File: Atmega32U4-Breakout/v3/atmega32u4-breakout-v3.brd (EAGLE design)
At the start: 39.1 x 21.3 mm, 57 parts, among them IC1 REG1117, U1 ATMEGA32U4

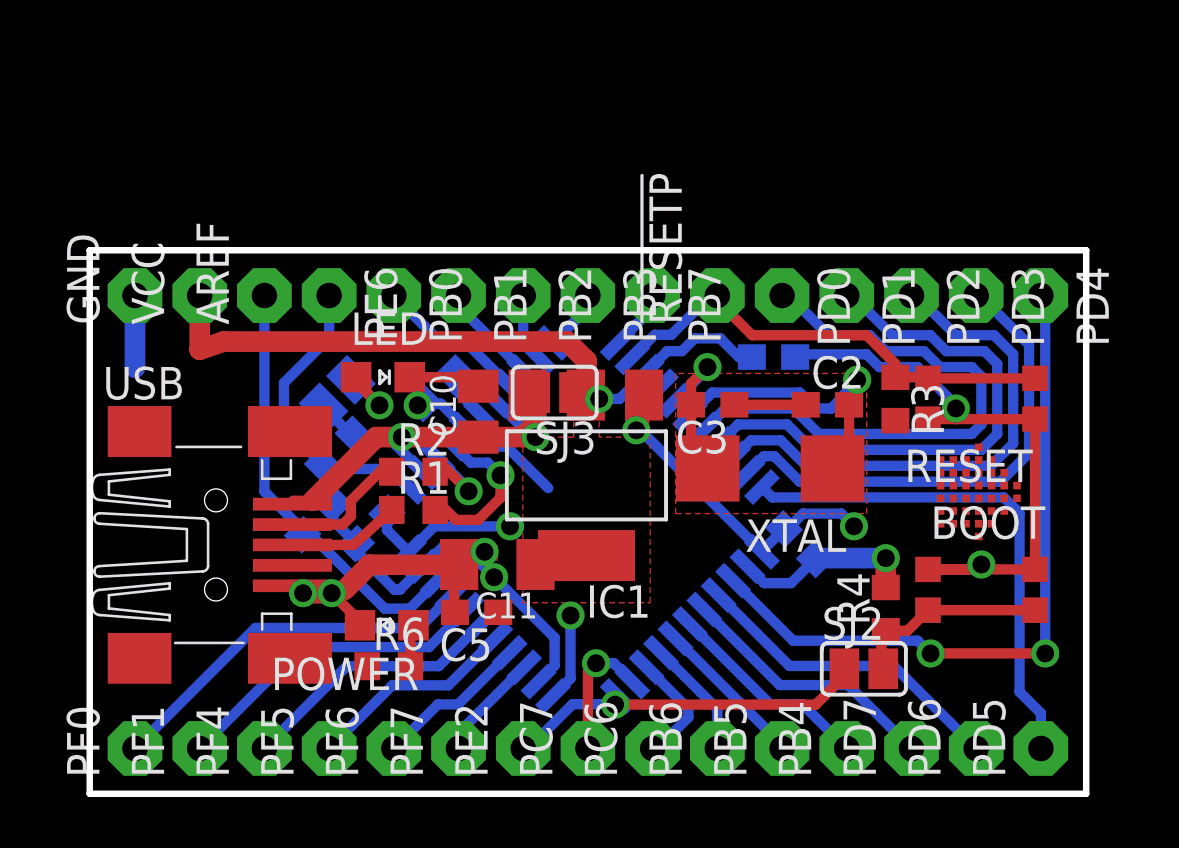
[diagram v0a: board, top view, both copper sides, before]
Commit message: Change button model, make vias smaller, adapt to multi-circuit-boards design rules, lots of small routing changes
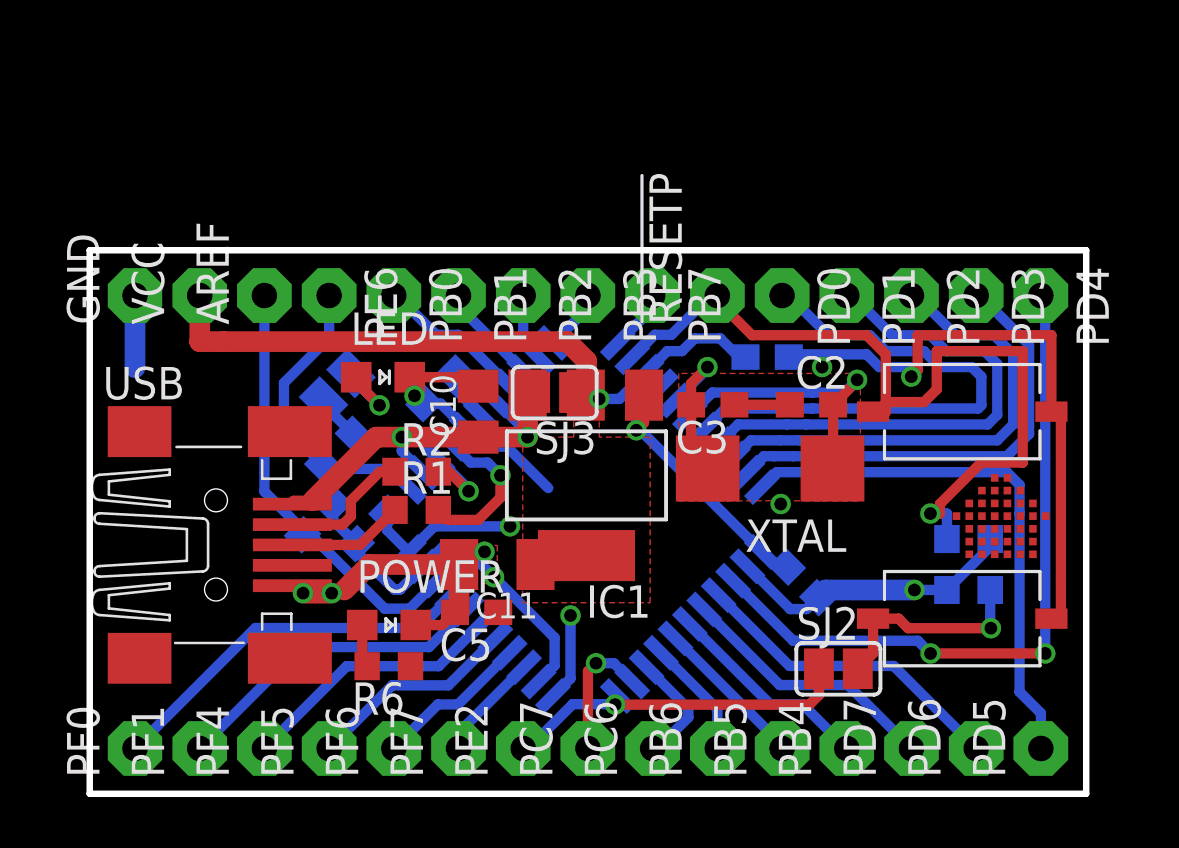
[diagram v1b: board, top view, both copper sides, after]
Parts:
- removed BOOT, RESET: SMDSWITCHKMR2NG, jocki:KMR2NG
- added BOOT1, RESET1: SMDSWITCHEDRAGON1, jocki:EDRAGON1
- moved R3 6.21 mm to (34.5, 10.0), flipped to the bottom, turned to 180 degrees
- moved R4 3.34 mm to (34.5, 8.00), flipped to the bottom, turned to 0 degrees
- moved C8 1.51 mm to (28.0, 8.30)
- moved SJ2 1.00 mm to (29.4, 4.91)
- moved C2 0.62 mm to (28.3, 15.3)
- moved C6 0.25 mm to (26.6, 17.1)
- moved SJ1 0.25 mm to (9.72, 16.0)
- moved R1 0.12 mm to (12.8, 11.1)
- moved R2 0.12 mm to (12.8, 12.6)
- moved POWER 0.09 mm to (11.8, 6.62), turned to 270 degrees
- turned R6 to 180 degrees
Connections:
- net !RESET: now also RESET1.P$2; no longer RESET.B1, RESET.B2
- net GND: now also BOOT1.P$1, RESET1.P$1; no longer BOOT.A1, BOOT.A2, RESET.A1, RESET.A2
- net N$21: now also BOOT1.P$2; no longer BOOT.B1, BOOT.B2
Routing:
- net !RESET: track 18.6 -> 32.9 mm, vias 0 -> 1
- net GND: track 81.2 -> 74.6 mm
- net VCC: track 43.9 -> 47.5 mm
- net VUSB: track 17.6 -> 16.1 mm
- net N$30: track 19.3 -> 18.1 mm
- net N$29: track 20.5 -> 19.2 mm
- net N$27: track 22.8 -> 21.5 mm
- net N$28: track 21.7 -> 20.4 mm
- net N$5: track 12.3 -> 11.0 mm
- net N$12: track 20.1 -> 21.3 mm
- net !HWB: track 14.5 -> 14.0 mm
- net N$21: track 8.29 -> 8.51 mm, vias 0 -> 1
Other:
- board text removed: "BOOT_EN"

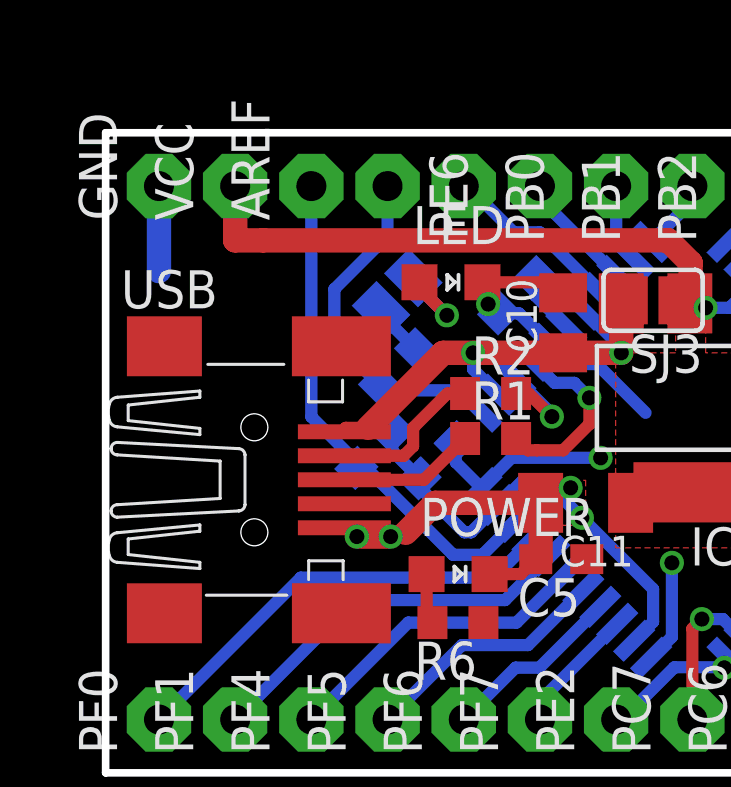
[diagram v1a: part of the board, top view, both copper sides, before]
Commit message: change USB plug package, rearrange bottom solder jumper
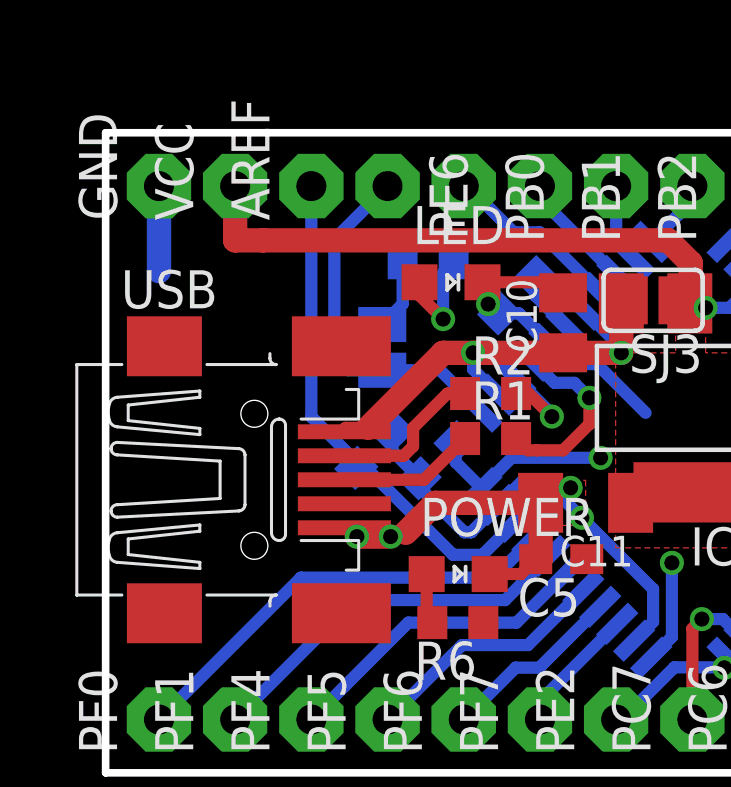
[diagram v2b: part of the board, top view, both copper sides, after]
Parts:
- USB: value MINI-USB-HIROSE-NOVIA -> MINI-USB-32005-201; device jocki:SMD-HIROSE-NOVIA -> jocki:32005-201
- moved R5 3.63 mm to (10.8, 17.0), turned to 180 degrees
- moved SJ1 1.84 mm to (9.22, 14.2), turned to 90 degrees
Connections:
- removed net N$4: R5.2, SJ1.1
- new net N$22: LED.A, R5.2
- net LED: now also SJ1.1; no longer R5.1
- net N$11: now also R5.1; no longer LED.A
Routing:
- net N$22: track 0.00 -> 3.57 mm, vias 0 -> 1
- net N$4: track 1.91 -> 0.00 mm
- net N$11: track 3.19 -> 2.34 mm, vias 1 -> 0
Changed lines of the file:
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@@
 <element name="C1" library="rcl" package="C0603" value="1u" x="13.718" y="15.918" rot="MR135"/>
 <element name="XTAL" library="jocki" package="ABM7" value="16MHz" x="26.708" y="12.768" rot="R180"/>
-<element name="USB" library="jocki" package="SMD-HIROSE-NOVIA" value="MINI-USB-HIROSE-NOVIA" x="4.958" y="9.768"/>
+<element name="USB" library="jocki" package="32005-201" value="MINI-USB-32005-201" x="4.958" y="9.768"/>
 <element name="C2" library="rcl" package="C0603" value="18p" x="28.333" y="15.268"/>
 <element name="C3" library="rcl" package="C0603" value="18p" x="24.458" y="15.268" rot="R180"/>
@@
 <element name="GND" library="jocki" package="2,15/1,0-NOPLACE" value="WIREPAD2,15/1,0-NOPLACE" x="1.778" y="19.558" rot="R90"/>
 <element name="VCC" library="jocki" package="2,15/1,0-NOPLACE" value="WIREPAD2,15/1,0-NOPLACE" x="4.318" y="19.558" rot="R90"/>
-<element name="R5" library="rcl" package="R0603" value="180" x="9.75" y="13.5113125" rot="MR135"/>
+<element name="R5" library="rcl" package="R0603" value="180" x="10.75" y="17" rot="MR180"/>
 <element name="R6" library="rcl" package="R0603" value="150" x="11.742" y="5.008" rot="R180"/>
-<element name="SJ1" library="jumper" package="SJ" value="" x="9.718" y="15.958" rot="MR135"/>
+<element name="SJ1" library="jumper" package="SJ" value="" x="9.220459375" y="14.18250625" rot="MR90"/>
 <element name="LED" library="led" package="CHIPLED_0805" value="RED" x="11.512" y="16.352" rot="R270"/>
 <element name="POWER" library="led" package="CHIPLED_0805" value="GREEN" x="11.75" y="6.625" rot="R270"/>
@@
 <contactref element="U1" pad="1"/>
 <contactref element="PE6" pad="1"/>
-<contactref element="R5" pad="1"/>
-<wire x1="7.625" y1="14.434228125" x2="7.625" y2="16.125" width="0.4064" layer="16"/>
-<wire x1="7.625" y1="16.125" x2="9.398" y2="17.898" width="0.4064" layer="16"/>
-<wire x1="9.398" y1="17.898" x2="9.398" y2="19.558" width="0.4064" layer="16"/>
-<wire x1="9.148959375" y1="12.91026875" x2="9.148959375" y2="12.851040625" width="0.4064" layer="16"/>
-<wire x1="9.148959375" y1="12.851040625" x2="9.25" y2="12.75" width="0.4064" layer="16"/>
-<wire x1="9.25" y1="12.75" x2="11.819146875" y2="12.75" width="0.4064" layer="16"/>
-<wire x1="11.819146875" y1="12.75" x2="12.52835625" y2="12.040790625" width="0.4064" layer="16"/>
-<wire x1="7.625" y1="14.434228125" x2="9.148959375" y2="12.91026875" width="0.4064" layer="16"/>
+<contactref element="SJ1" pad="1"/>
+<wire x1="12.52835625" y1="12.040790625" x2="11.148640625" y2="13.42050625" width="0.4064" layer="16"/>
+<wire x1="11.148640625" y1="13.42050625" x2="9.220459375" y2="13.42050625" width="0.4064" layer="16"/>
+<wire x1="9.220459375" y1="13.42050625" x2="8.07949375" y2="13.42050625" width="0.4064" layer="16"/>
+<wire x1="8.07949375" y1="13.42050625" x2="7.625" y2="13.875" width="0.4064" layer="16"/>
+<wire x1="7.625" y1="13.875" x2="7.625" y2="17.785" width="0.4064" layer="16"/>
+<wire x1="7.625" y1="17.785" x2="9.398" y2="19.558" width="0.4064" layer="16"/>
 </signal>
 <signal name="N$12">
@@
 <via x="17.1886" y="14" extent="1-16" drill="0.5" shape="octagon"/>
 </signal>
-<signal name="N$4">
-<contactref element="R5" pad="2"/>
-<contactref element="SJ1" pad="1"/>
-<wire x1="10.35104375" y1="14.112353125" x2="10.23601875" y2="14.112353125" width="0.4064" layer="16"/>
-<wire x1="9.1791875" y1="15.419184375" x2="9.1791875" y2="15.284209375" width="0.4064" layer="16"/>
-<wire x1="9.1791875" y1="15.284209375" x2="10.35104375" y2="14.112353125" width="0.4064" layer="16"/>
-</signal>
 <signal name="N$11">
 <contactref element="SJ1" pad="2"/>
+<contactref element="R5" pad="1"/>
+<wire x1="9.220459375" y1="14.94450625" x2="9.9" y2="15.624046875" width="0.4064" layer="16"/>
+<wire x1="9.9" y1="15.624046875" x2="9.9" y2="17" width="0.4064" layer="16"/>
+</signal>
+<signal name="N$22">
+<contactref element="R5" pad="2"/>
 <contactref element="LED" pad="A"/>
-<via x="11.375" y="15.25" extent="1-16" drill="0.5"/>
-<wire x1="10.462" y1="16.352" x2="10.462" y2="16.163" width="0.4064" layer="1"/>
-<wire x1="10.462" y1="16.163" x2="11.375" y2="15.25" width="0.4064" layer="1"/>
-<wire x1="10.256815625" y1="16.4968125" x2="10.256815625" y2="16.368184375" width="0.4064" layer="16"/>
-<wire x1="10.256815625" y1="16.368184375" x2="11.375" y2="15.25" width="0.4064" layer="16"/>
+<via x="11.25" y="15.125" extent="1-16" drill="0.5"/>
+<wire x1="11.25" y1="15.125" x2="10.462" y2="15.913" width="0.4064" layer="1"/>
+<wire x1="10.462" y1="15.913" x2="10.462" y2="16.352" width="0.4064" layer="1"/>
+<wire x1="11.6" y1="17" x2="11.25" y2="16.65" width="0.4064" layer="16"/>
+<wire x1="11.25" y1="16.65" x2="11.25" y2="15.125" width="0.4064" layer="16"/>
 </signal>
 </signals>

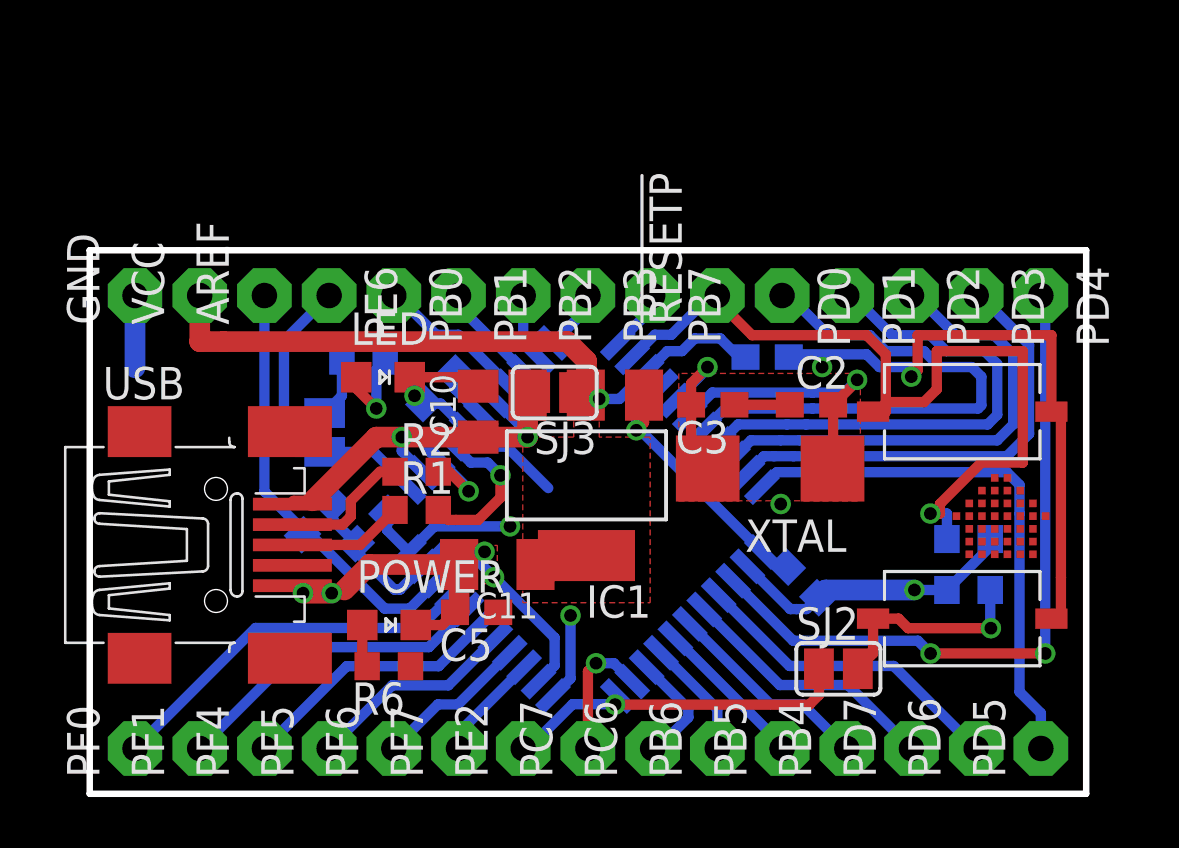
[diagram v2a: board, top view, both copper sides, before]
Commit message: Add resettable fuse, rearrange stuff
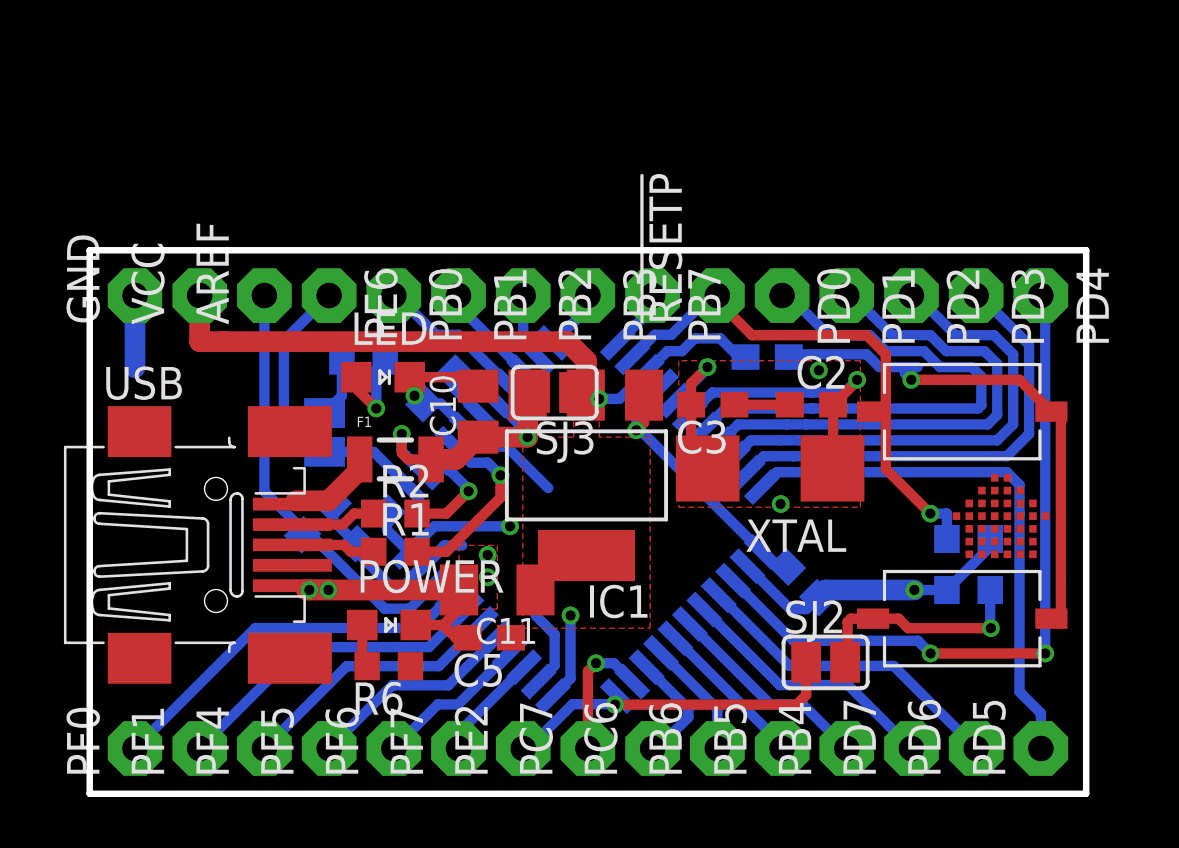
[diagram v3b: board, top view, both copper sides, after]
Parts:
- added F1: PTCSMD, SparkFun-PowerIC:PTC-1206
- moved R1 1.84 mm to (12.0, 9.50)
- moved R2 1.84 mm to (12.0, 11.0)
- moved C5 1.12 mm to (15.7, 6.12)
- moved C11 1.00 mm to (16.0, 8.00)
- moved SJ2 0.56 mm to (28.9, 5.16)
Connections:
- new net N$4: F1.1, USB.1
- net VUSB: now also F1.2; no longer USB.1
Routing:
- net !RESET: track 32.9 -> 21.5 mm
- net GND: track 74.6 -> 66.8 mm
- net VUSB: track 16.1 -> 12.0 mm
- net N$4: track 0.00 -> 3.60 mm
- net N$2: track 5.24 -> 3.37 mm
- net N$1: track 4.59 -> 3.30 mm
- net N$9: track 6.25 -> 7.44 mm
- net N$10: track 3.31 -> 4.19 mm
